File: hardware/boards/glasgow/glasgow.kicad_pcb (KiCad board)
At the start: 4 copper layers, 80 x 49 mm, 242 parts, among them J1 USB_C_Receptacle_USB2.0, J10 Conn_01x03, J2 Conn_02x10_Odd_Even, J3 Conn_02x10_Odd_Even, J4 Conn_01x02, J5 Conn_02x22_Odd_Even, J6 Conn_01x08, J7 Conn_01x08, J8 Conn_01x08, J9 Conn_01x08, U1 CY7C68013A-56LTX, U10 SN74LVC1T45DRL, U11 SN74LVC1T45DRL, U12 ADC081C021CIMM, U13 DAC081C081CIMK, U14 TPS73101DBV, U15 TPD3S014, U16 SN74LVC1T45DRL, U17 SN74LVC1T45DRL, U18 SN74LVC1T45DRL, U19 PCA6408APW, U2 CAT24M01W, U20 DAC081C081CIMK, U21 ADC081C021CIMM, U22 SN74LVC1T45DRL, U23 SN74LVC1T45DRL, U24 SN74LVC1T45DRL, U25 SN74LVC1T45DRL, U26 SN74LVC1T45DRL, U27 SN74LVC1T45DRL, U28 SN74LVC1T45DRL, U29 SN74LVC1T45DRL, U3 CAT24C256W, U30 ICE40HX8K-BG121, U31 TPS73101DBV, U32 SN74LVC1T45DRL, U33 MG2040, U34 ATECC508A, U35 MG2040, U36 TLV73312PQDRVRQ1, U4 SN74LVC1T45DRL, U5 PCA6408APW, U6 SN74LVC1T45DRL, U7 LM3880MF-1AF, U8 TLV75533PDRVR, U9 SN74LVC1T45DRL, Y1 24M

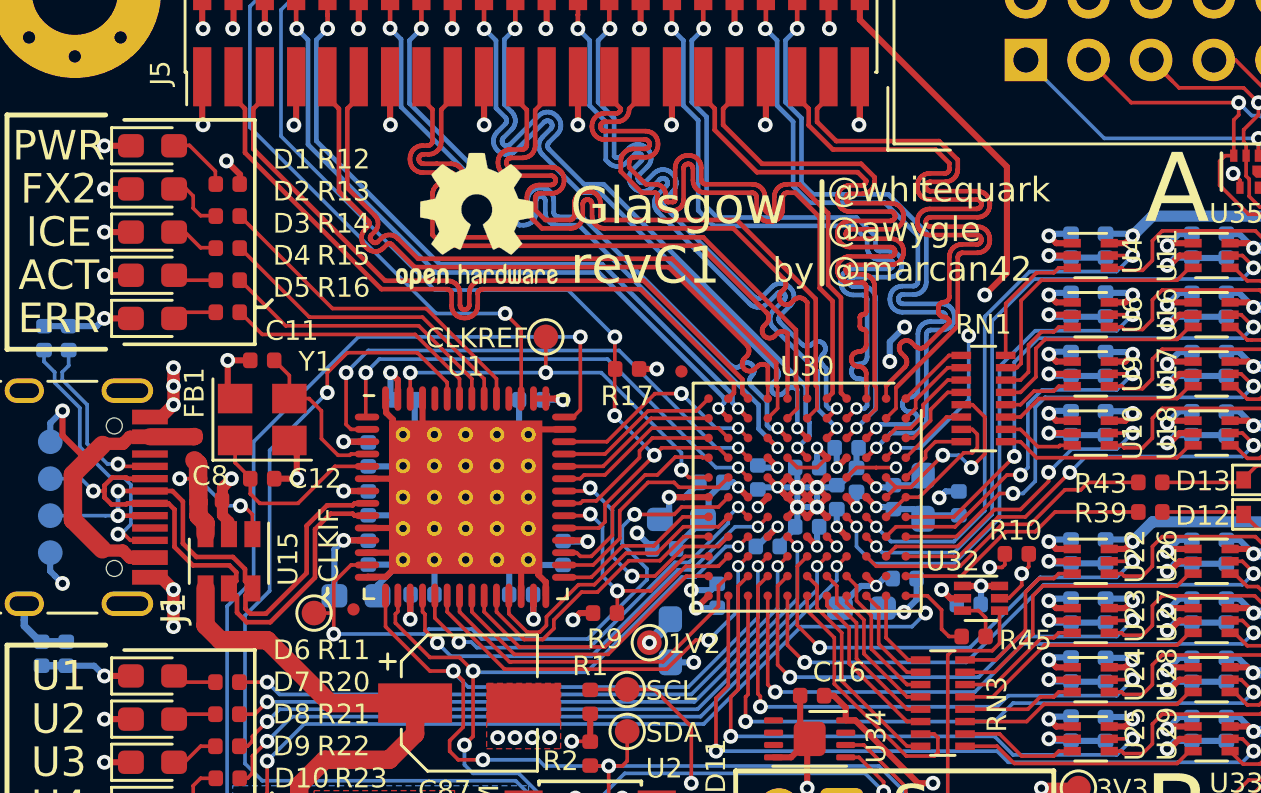
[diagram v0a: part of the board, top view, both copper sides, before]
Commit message: modified revC1 with a usb-c connector and custom silkscreen
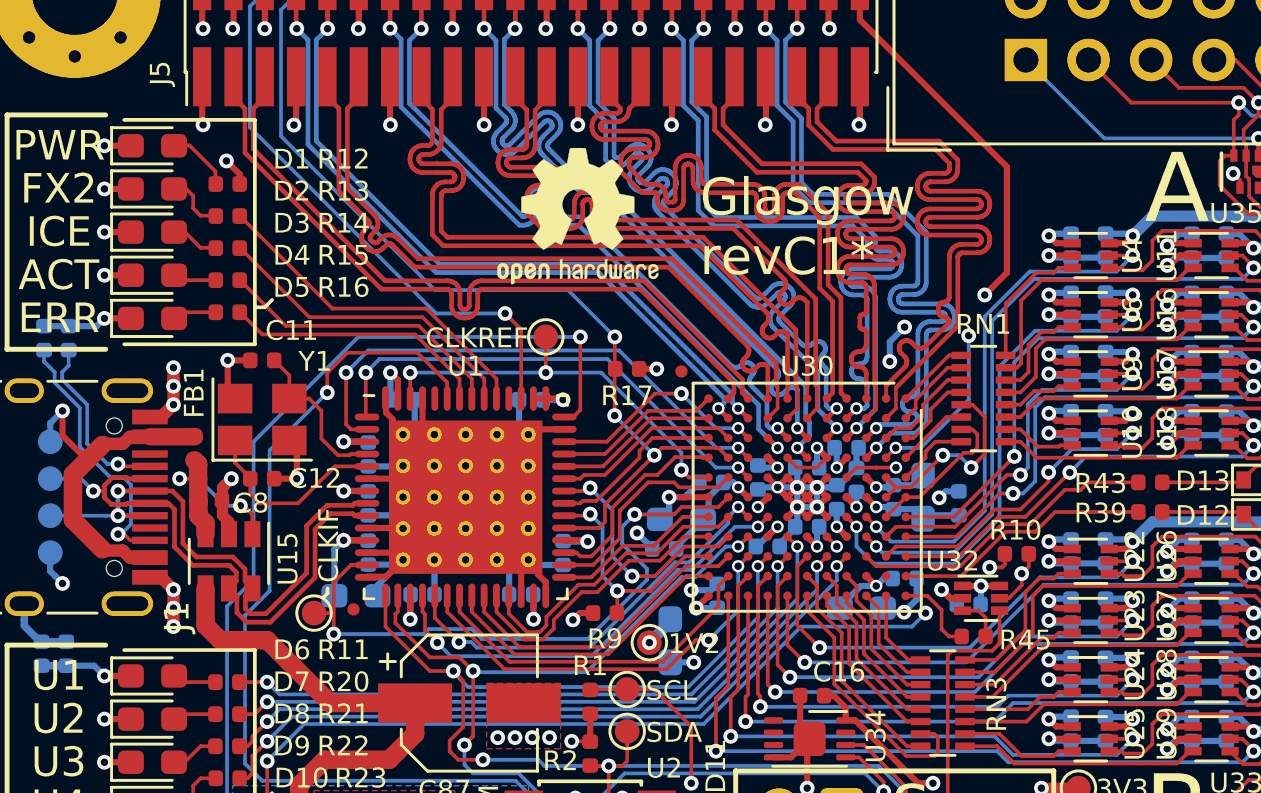
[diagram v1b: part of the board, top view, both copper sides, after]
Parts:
- removed NONO_HANA: MECHOKKU, Glasgow:nono_hana
- added G***: LOGO, silk:brasao2, B.Cu at (74.2, 80.2)
- moved REF** 4.10 mm to (74.4, 84.1)
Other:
- board text added: "@gimbas @FFY00"
- board text added: "Glasgow revC1*"
- board text added: "Rafael Silva Filipe Laíns"
- board text removed: "@whitequark @awygle @marcan42"
- board text removed: "Glasgow revC1"
- board text removed: "Serial No:"
- board text removed: "by"
